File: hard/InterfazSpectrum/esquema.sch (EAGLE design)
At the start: 17 parts, among them IC1 ATMEGA644-20PU, IC2 XC9572-PC44, IC3 LD1117, Q3 16 MHz, X1 ZX-EDGE

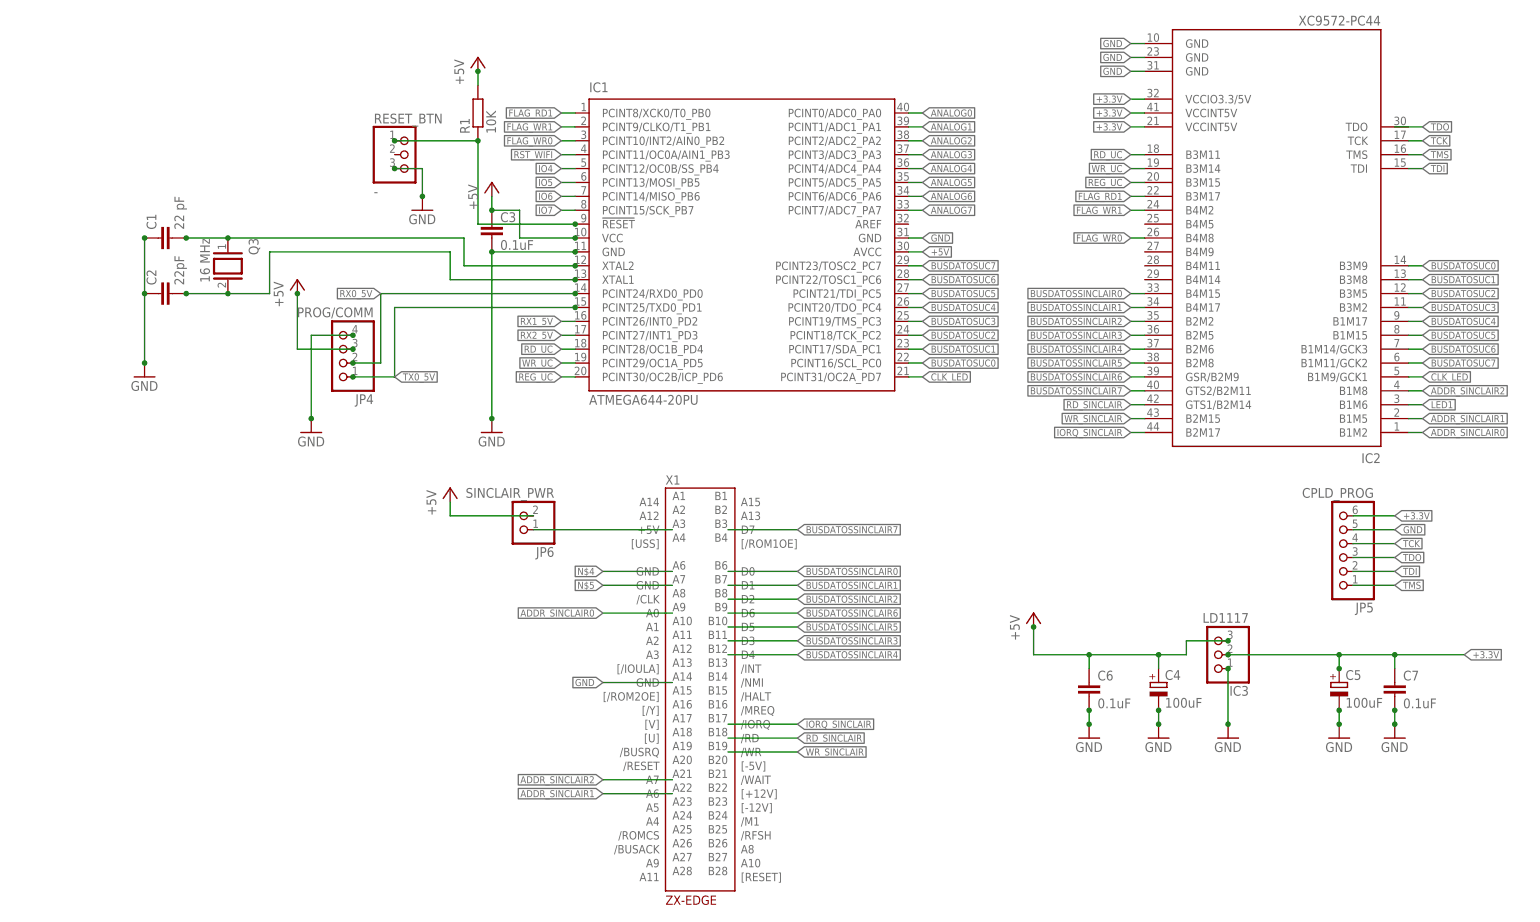
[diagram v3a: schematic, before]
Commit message: Esquema: Añadido módulo wifi y conectores I/O
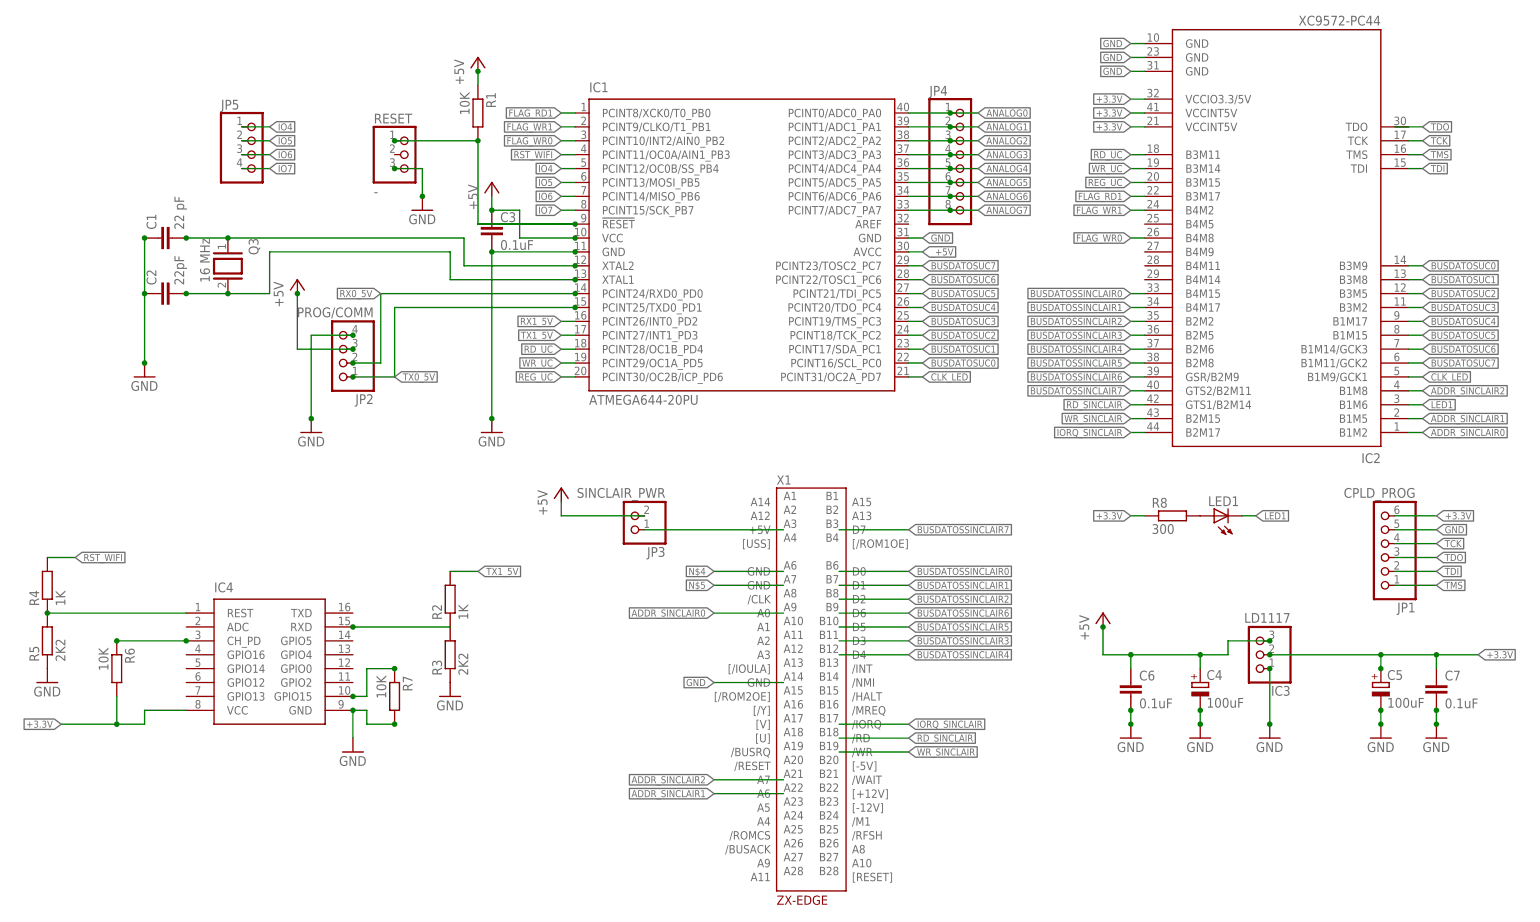
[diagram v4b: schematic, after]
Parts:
- removed JP6: SINCLAIR_PWR, pinhead:PINHD-1X2
- added IC4: ESP-07ESP-07, Esp-07:ESP-07ESP-07
- added JP1: CPLD_PROG, pinhead:PINHD-1X6
- added JP2: PROG/COMM, pinhead:PINHD-1X4
- added JP3: SINCLAIR_PWR, pinhead:PINHD-1X2
- added LED1: (no value), led:LED3MM
- added R2, R4: 1K, resistor:R-EU_0207_10
- added R3, R5: 2K2, resistor:R-EU_0207_10
- added R6, R7: 10K, resistor:R-EU_0207_10
- added R8: 300, resistor:R-EU_0207_10
- JP4: value PROG/COMM -> (none); device pinhead:PINHD-1X4 -> pinhead:PINHD-1X8
- JP5: value CPLD_PROG -> (none); device pinhead:PINHD-1X6 -> pinhead:PINHD-1X4
- renumbered RESET_BTN to RESET
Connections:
- removed net +5V: C3.1, C4.+, C6.1, IC1.AVCC, IC1.VCC, IC3.3, JP4.3, JP6.2, R1.2
- removed net RX2_5V: IC1.PCINT27/INT1_PD3
- new net CH_PH_PULLUP: IC4.CH_PD, R6.1
- new net GPIO15_PULLDOWN: IC4.GPIO15, R7.1
- new net N$1: IC4.RXD, R2.1, R3.2
- new net N$2: LED1.A, R8.2
- new net RST_WIFI_3.3V: IC4.REST, R4.1, R5.2
- new net TX1_5V: IC1.PCINT27/INT1_PD3, R2.2
- new net _+5V: C3.1, C4.+, C6.1, IC1.AVCC, IC1.VCC, IC3.3, JP2.3, JP3.2, R1.1
- net +3.3V: now also IC4.VCC, JP1.6, R6.2, R8.1; no longer JP5.6
- net ANALOG0: now also JP4.1
- net ANALOG1: now also JP4.2
- net ANALOG2: now also JP4.3
- net ANALOG3: now also JP4.4
- net ANALOG4: now also JP4.5
- net ANALOG5: now also JP4.6
- net ANALOG6: now also JP4.7
- net ANALOG7: now also JP4.8
- net GND: now also IC4.GND, JP1.5, JP2.4, R3.1, R5.1, R7.2; no longer JP4.4, JP5.5
- net IO4: now also JP5.1
- net IO5: now also JP5.2
- net IO6: now also JP5.3
- net IO7: now also JP5.4
- net LED1: now also LED1.C
- net N$3: now also JP3.1; no longer JP6.1
- net RESET_UC: now also R1.2; no longer R1.1
- net RST_WIFI: now also R4.2
- net RX0_5V: now also JP2.2; no longer JP4.2
- net TCK: now also JP1.4; no longer JP5.4
- net TDI: now also JP1.2; no longer JP5.2
- net TDO: now also JP1.3; no longer JP5.3
- net TMS: now also JP1.1; no longer JP5.1
- net TX0_5V: now also JP2.1; no longer JP4.1
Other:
- moved on the sheet: C4, C5, C6, C7, IC3, R1, X1

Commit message: Arregladas algunas señales que no estaban conectadas en el cpld, módulo wifi y conector edge.
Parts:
- R8: value 300 -> 1K
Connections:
- net _+5V renamed +5V
- removed net N$4: X1.GND@1
- removed net N$5: X1.GND@2
- net GND: now also X1.GND@1, X1.GND@2
- net RX1_5V: now also IC4.TXD
- net TDO: now also IC2.TDO
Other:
- moved on the sheet: C3, R1, RESET
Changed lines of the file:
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@@
 <part name="R6" library="resistor" deviceset="R-EU_" device="0207_10" value="10K"/>
 <part name="R7" library="resistor" deviceset="R-EU_" device="0207_10" value="10K"/>
-<part name="R8" library="resistor" deviceset="R-EU_" device="0207_10" value="300"/>
+<part name="R8" library="resistor" deviceset="R-EU_" device="0207_10" value="1K"/>
 <part name="LED1" library="led" deviceset="LED" device="3MM"/>
 </parts>
@@
 <instances>
 <instance part="Q3" gate="G$1" x="53.34" y="114.3" rot="R270"/>
-<instance part="P+1" gate="1" x="99.06" y="152.4"/>
-<instance part="GND1" gate="1" x="101.6" y="83.82"/>
+<instance part="P+1" gate="1" x="96.52" y="152.4"/>
+<instance part="GND1" gate="1" x="93.98" y="83.82"/>
 <instance part="GND2" gate="1" x="38.1" y="93.98"/>
-<instance part="P+2" gate="1" x="101.6" y="129.54"/>
+<instance part="P+2" gate="1" x="93.98" y="132.08"/>
 <instance part="C1" gate="G$1" x="40.64" y="119.38" rot="R90"/>
 <instance part="C2" gate="G$1" x="40.64" y="109.22" rot="R90"/>
-<instance part="GND3" gate="1" x="88.9" y="124.46"/>
+<instance part="GND3" gate="1" x="83.82" y="124.46"/>
 <instance part="IC1" gate="G$1" x="147.32" y="119.38"/>
 <instance part="JP2" gate="A" x="73.66" y="99.06" rot="R180"/>
-<instance part="RESET" gate="A" x="86.36" y="134.62"/>
+<instance part="RESET" gate="A" x="81.28" y="134.62"/>
 <instance part="GND9" gate="1" x="68.58" y="83.82"/>
 <instance part="P+7" gate="1" x="66.04" y="111.76"/>
@@
 <instance part="GND7" gate="1" x="218.44" y="27.94"/>
 <instance part="GND8" gate="1" x="274.32" y="27.94"/>
-<instance part="C3" gate="G$1" x="101.6" y="121.92"/>
+<instance part="C3" gate="G$1" x="93.98" y="124.46"/>
 <instance part="JP1" gate="A" x="264.16" y="63.5" rot="R180"/>
 <instance part="X1" gate="ZX-BUS" x="160.02" y="60.96"/>
@@
 <instance part="JP4" gate="A" x="187.96" y="132.08"/>
 <instance part="JP5" gate="A" x="58.42" y="134.62"/>
-<instance part="R1" gate="G$1" x="99.06" y="142.24" rot="R270"/>
+<instance part="R1" gate="G$1" x="96.52" y="142.24" rot="R270"/>
 <instance part="R2" gate="G$1" x="93.98" y="53.34" rot="R90"/>
 <instance part="R3" gate="G$1" x="93.98" y="43.18" rot="R90"/>
@@
 <net name="OSC1" class="0">
 <segment>
-<wire x1="53.34" y1="119.38" x2="96.52" y2="119.38" width="0.1524" layer="91"/>
-<wire x1="96.52" y1="119.38" x2="96.52" y2="114.3" width="0.1524" layer="91"/>
-<wire x1="96.52" y1="114.3" x2="116.84" y2="114.3" width="0.1524" layer="91"/>
+<wire x1="53.34" y1="119.38" x2="86.36" y2="119.38" width="0.1524" layer="91"/>
+<wire x1="86.36" y1="119.38" x2="86.36" y2="114.3" width="0.1524" layer="91"/>
+<wire x1="86.36" y1="114.3" x2="116.84" y2="114.3" width="0.1524" layer="91"/>
 <wire x1="53.34" y1="119.38" x2="45.72" y2="119.38" width="0.1524" layer="91"/>
 <junction x="53.34" y="119.38"/>
@@
 <wire x1="53.34" y1="109.22" x2="60.96" y2="109.22" width="0.1524" layer="91"/>
 <wire x1="60.96" y1="109.22" x2="60.96" y2="116.84" width="0.1524" layer="91"/>
-<wire x1="60.96" y1="116.84" x2="93.98" y2="116.84" width="0.1524" layer="91"/>
-<wire x1="93.98" y1="116.84" x2="93.98" y2="111.76" width="0.1524" layer="91"/>
-<wire x1="93.98" y1="111.76" x2="116.84" y2="111.76" width="0.1524" layer="91"/>
+<wire x1="60.96" y1="116.84" x2="83.82" y2="116.84" width="0.1524" layer="91"/>
+<wire x1="83.82" y1="116.84" x2="83.82" y2="111.76" width="0.1524" layer="91"/>
+<wire x1="83.82" y1="111.76" x2="116.84" y2="111.76" width="0.1524" layer="91"/>
 <junction x="116.84" y="111.76"/>
 <junction x="53.34" y="109.22"/>
@@
 </segment>
 <segment>
-<wire x1="101.6" y1="86.36" x2="101.6" y2="116.84" width="0.1524" layer="91"/>
-<wire x1="101.6" y1="116.84" x2="116.84" y2="116.84" width="0.1524" layer="91"/>
+<wire x1="93.98" y1="86.36" x2="93.98" y2="116.84" width="0.1524" layer="91"/>
+<junction x="93.98" y="86.36"/>
+<pinref part="GND1" gate="1" pin="GND"/>
+<pinref part="C3" gate="G$1" pin="2"/>
+<pinref part="IC1" gate="G$1" pin="GND"/>
+<wire x1="93.98" y1="116.84" x2="93.98" y2="119.38" width="0.1524" layer="91"/>
+<wire x1="116.84" y1="116.84" x2="93.98" y2="116.84" width="0.1524" layer="91"/>
+<junction x="93.98" y="116.84"/>
 <junction x="116.84" y="116.84"/>
-<junction x="101.6" y="86.36"/>
-<pinref part="GND1" gate="1" pin="GND"/>
-<pinref part="IC1" gate="G$1" pin="GND"/>
-<pinref part="C3" gate="G$1" pin="2"/>
-<junction x="101.6" y="116.84"/>
-</segment>
-<segment>
-<wire x1="88.9" y1="132.08" x2="83.82" y2="132.08" width="0.1524" layer="91"/>
-<wire x1="88.9" y1="127" x2="88.9" y2="132.08" width="0.1524" layer="91"/>
-<junction x="83.82" y="132.08"/>
-<junction x="88.9" y="127"/>
+</segment>
+<segment>
+<wire x1="83.82" y1="132.08" x2="78.74" y2="132.08" width="0.1524" layer="91"/>
+<wire x1="83.82" y1="127" x2="83.82" y2="132.08" width="0.1524" layer="91"/>
+<junction x="78.74" y="132.08"/>
+<junction x="83.82" y="127"/>
 <pinref part="RESET" gate="A" pin="3"/>
 <pinref part="GND3" gate="1" pin="GND"/>
@@
 <junction x="83.82" y="30.48"/>
 </segment>
-</net>
-<net name="_+5V" class="2">
-<segment>
-<wire x1="99.06" y1="149.86" x2="99.06" y2="147.32" width="0.1524" layer="91"/>
-<junction x="99.06" y="149.86"/>
+<segment>
+<pinref part="X1" gate="ZX-BUS" pin="GND@1"/>
+<wire x1="154.94" y1="58.42" x2="142.24" y2="58.42" width="0.1524" layer="91"/>
+<label x="142.24" y="58.42" size="1.27" layer="95" rot="R180" xref="yes"/>
+</segment>
+<segment>
+<pinref part="X1" gate="ZX-BUS" pin="GND@2"/>
+<wire x1="154.94" y1="55.88" x2="142.24" y2="55.88" width="0.1524" layer="91"/>
+<label x="142.24" y="55.88" size="1.27" layer="95" rot="R180" xref="yes"/>
+</segment>
+</net>
+<net name="+5V" class="2">
+<segment>
+<wire x1="96.52" y1="149.86" x2="96.52" y2="147.32" width="0.1524" layer="91"/>
+<junction x="96.52" y="149.86"/>
 <pinref part="P+1" gate="1" pin="+5V"/>
 <pinref part="R1" gate="G$1" pin="1"/>
 </segment>
 <segment>
-<wire x1="101.6" y1="127" x2="101.6" y2="124.46" width="0.1524" layer="91"/>
-<wire x1="101.6" y1="124.46" x2="106.68" y2="124.46" width="0.1524" layer="91"/>
-<wire x1="106.68" y1="124.46" x2="106.68" y2="119.38" width="0.1524" layer="91"/>
-<wire x1="106.68" y1="119.38" x2="116.84" y2="119.38" width="0.1524" layer="91"/>
+<wire x1="93.98" y1="129.54" x2="93.98" y2="127" width="0.1524" layer="91"/>
+<wire x1="93.98" y1="127" x2="104.14" y2="127" width="0.1524" layer="91"/>
+<wire x1="104.14" y1="127" x2="104.14" y2="119.38" width="0.1524" layer="91"/>
+<wire x1="104.14" y1="119.38" x2="116.84" y2="119.38" width="0.1524" layer="91"/>
 <junction x="116.84" y="119.38"/>
 <pinref part="P+2" gate="1" pin="+5V"/>
 <pinref part="IC1" gate="G$1" pin="VCC"/>
 <pinref part="C3" gate="G$1" pin="1"/>
-<junction x="101.6" y="124.46"/>
+<junction x="93.98" y="127"/>
 </segment>
 <segment>
@@
 <label x="114.3" y="104.14" size="1.27" layer="95" rot="R180" xref="yes"/>
 </segment>
+<segment>
+<pinref part="IC4" gate="G$1" pin="TXD"/>
+<wire x1="76.2" y1="50.8" x2="78.74" y2="50.8" width="0.1524" layer="91"/>
+<label x="78.74" y="50.8" size="1.27" layer="95" xref="yes"/>
+</segment>
 </net>
 <net name="TX1_5V" class="0">
@@
 <net name="TDO" class="0">
 <segment>
-<wire x1="266.7" y1="139.7" x2="271.78" y2="139.7" width="0.1524" layer="91"/>
-<label x="271.78" y="139.7" size="1.27" layer="95" xref="yes"/>
-</segment>
-<segment>
 <pinref part="JP1" gate="A" pin="3"/>
 <wire x1="266.7" y1="60.96" x2="274.32" y2="60.96" width="0.1524" layer="91"/>
 <label x="274.32" y="60.96" size="1.27" layer="95" xref="yes"/>
+</segment>
+<segment>
+<pinref part="IC2" gate="P" pin="TDO"/>
+<wire x1="269.24" y1="139.7" x2="271.78" y2="139.7" width="0.1524" layer="91"/>
+<label x="271.78" y="139.7" size="1.27" layer="95" xref="yes"/>
 </segment>
 </net>
@@
 <net name="RESET_UC" class="0">
 <segment>
-<wire x1="116.84" y1="121.92" x2="99.06" y2="121.92" width="0.1524" layer="91"/>
-<wire x1="99.06" y1="121.92" x2="99.06" y2="137.16" width="0.1524" layer="91"/>
-<wire x1="83.82" y1="137.16" x2="99.06" y2="137.16" width="0.1524" layer="91"/>
-<junction x="83.82" y="137.16"/>
+<wire x1="106.68" y1="121.92" x2="106.68" y2="129.54" width="0.1524" layer="91"/>
+<wire x1="106.68" y1="129.54" x2="101.6" y2="129.54" width="0.1524" layer="91"/>
+<wire x1="101.6" y1="129.54" x2="101.6" y2="137.16" width="0.1524" layer="91"/>
+<wire x1="101.6" y1="137.16" x2="96.52" y2="137.16" width="0.1524" layer="91"/>
+<wire x1="78.74" y1="137.16" x2="96.52" y2="137.16" width="0.1524" layer="91"/>
+<junction x="78.74" y="137.16"/>
 <junction x="116.84" y="121.92"/>
 <pinref part="RESET" gate="A" pin="1"/>
 <pinref part="IC1" gate="G$1" pin="!RESET"/>
 <pinref part="R1" gate="G$1" pin="2"/>
-<junction x="99.06" y="137.16"/>
-<wire x1="116.84" y1="121.92" x2="99.06" y2="121.92" width="0.1524" layer="91"/>
-</segment>
-</net>
-<net name="N$4" class="0">
-<segment>
-<pinref part="X1" gate="ZX-BUS" pin="GND@1"/>
-<wire x1="154.94" y1="58.42" x2="142.24" y2="58.42" width="0.1524" layer="91"/>
-<label x="142.24" y="58.42" size="1.27" layer="95" rot="R180" xref="yes"/>
-</segment>
-</net>
-<net name="N$5" class="0">
-<segment>
-<pinref part="X1" gate="ZX-BUS" pin="GND@2"/>
-<wire x1="154.94" y1="55.88" x2="142.24" y2="55.88" width="0.1524" layer="91"/>
-<label x="142.24" y="55.88" size="1.27" layer="95" rot="R180" xref="yes"/>
+<junction x="96.52" y="137.16"/>
+<wire x1="116.84" y1="121.92" x2="106.68" y2="121.92" width="0.1524" layer="91"/>
 </segment>
 </net>
@@
 <wire x1="93.98" y1="48.26" x2="76.2" y2="48.26" width="0.1524" layer="91"/>
 <junction x="76.2" y="48.26"/>
+<junction x="93.98" y="48.26"/>
 </segment>
 </net>
@@
 </sheet>
 </sheets>
+<errors>
+</errors>
 </schematic>
 </drawing>

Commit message: Modificada resistencia R8, el valor correcto es 300 Ohm
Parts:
- R8: value 1K -> 300
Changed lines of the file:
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@@
 <part name="R6" library="resistor" deviceset="R-EU_" device="0207_10" value="10K"/>
 <part name="R7" library="resistor" deviceset="R-EU_" device="0207_10" value="10K"/>
-<part name="R8" library="resistor" deviceset="R-EU_" device="0207_10" value="1K"/>
+<part name="R8" library="resistor" deviceset="R-EU_" device="0207_10" value="300"/>
 <part name="LED1" library="led" deviceset="LED" device="3MM"/>
 </parts>
